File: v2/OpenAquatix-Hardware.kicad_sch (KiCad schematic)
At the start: 3 parts

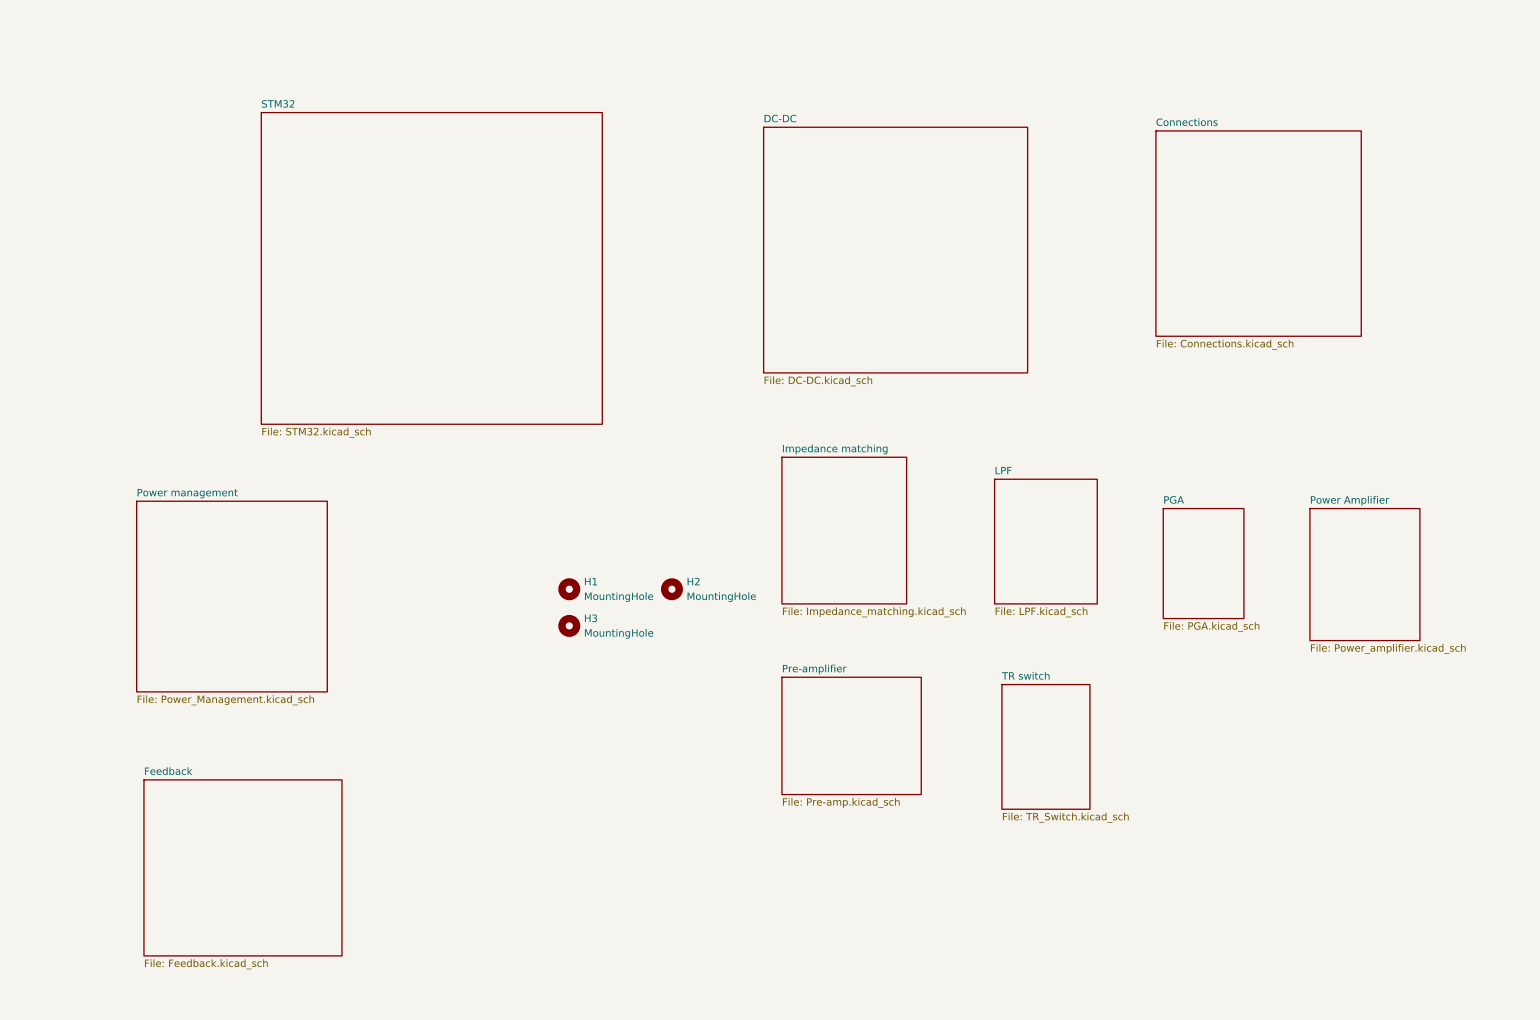
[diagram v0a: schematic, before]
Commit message: Most v2 changes made
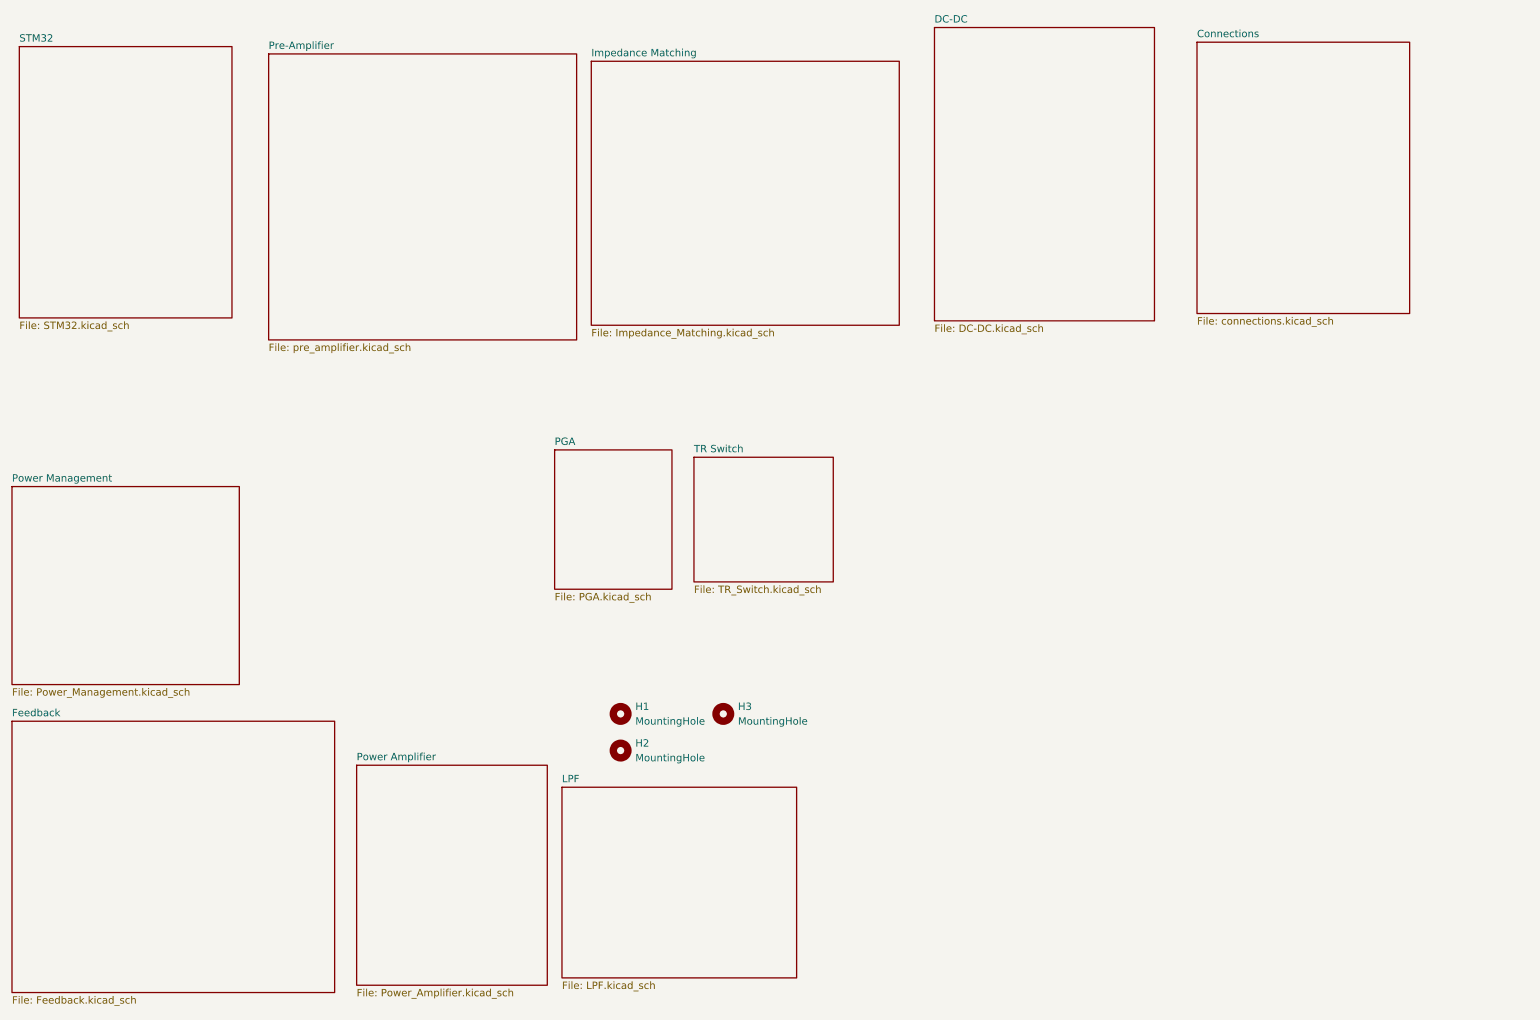
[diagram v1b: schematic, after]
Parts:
- renumbered H3 to H2, H2 to H3
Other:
- removed sheet Impedance matching
- removed sheet Power management
- removed sheet Pre-amplifier
- removed sheet TR switch
- added sheet Impedance Matching (Impedance_Matching.kicad_sch)
- added sheet Power Management (Power_Management.kicad_sch)
- added sheet Pre-Amplifier (pre_amplifier.kicad_sch)
- added sheet TR Switch (TR_Switch.kicad_sch)
- sheet Connections: file Connections.kicad_sch -> connections.kicad_sch
- sheet Power Amplifier: file Power_amplifier.kicad_sch -> Power_Amplifier.kicad_sch
- title: (none) -> OpenAquatix Main Board Hardware
- moved on the sheet: H1, H2, H3
